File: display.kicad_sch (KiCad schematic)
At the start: 65 parts, among them IC11 SN74LV1T125DBVR, IC18 TPD8S009DSMR, IC2 TPD8S009DSMR, IC6 PCA9517ADP, J1 HDMI-Micro-D_Molex_467561001, J15 Bus_DDR4_SODIMM_CUSTOM_Jetson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, J2 DisplayPort-Mini_TE_2129320-3, T1 BSS138PW

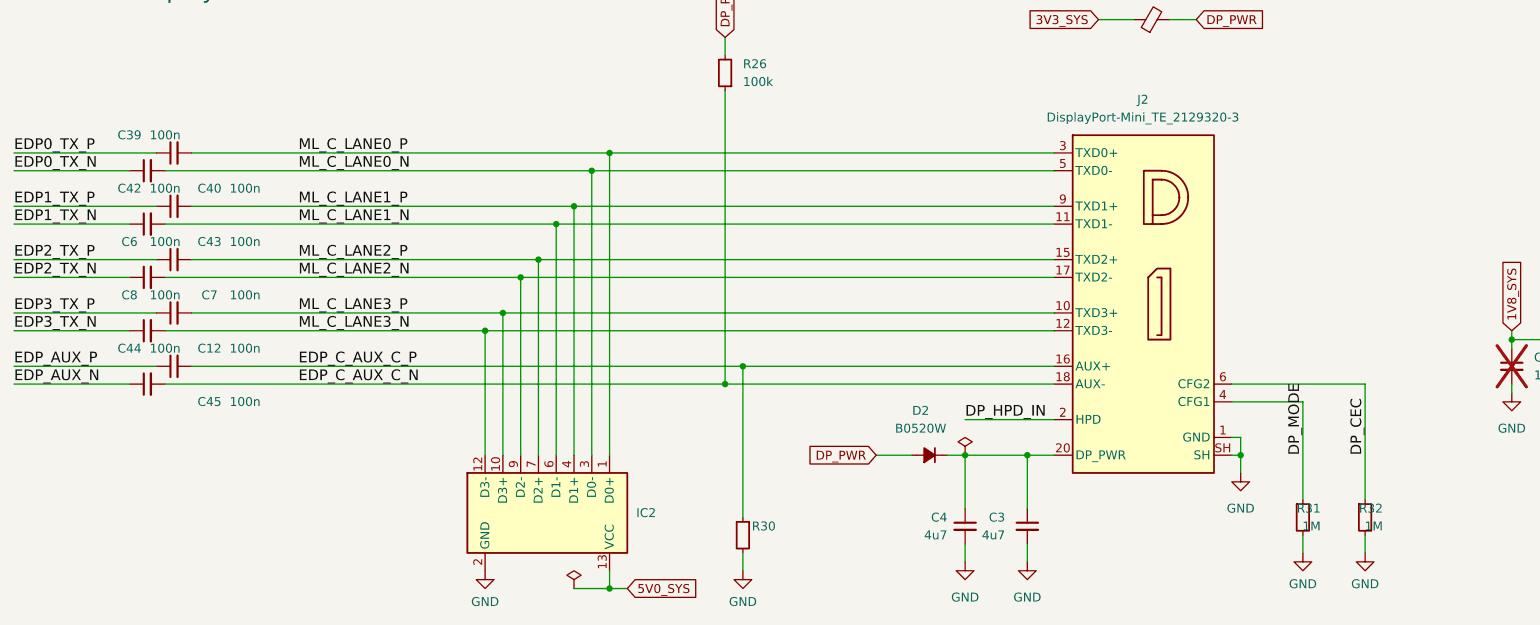
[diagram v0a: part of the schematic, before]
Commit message: fix(sch): resolve all symbol, label, property, and syntax collisions on Supply sheet (Page 6)
Fix unquoted COMP pin name in SIC477ED-T1-GE3, relocate #FLG0313 and #FLG0312 PWR_FLAGs, move R93/C61/R96/R76/R44/R70/L1/U1/U5/IC4/U3 properties out of bodies and wires, fix R117 table box, hide J4 duplicate Description, remove duplicate PWR_EN label and J12 MP1/MP2 no_connect conflicts, and delete stray off-sheet artifacts.

Co-Authored-By: CopperPilot <noreply@copperpilot.ai>
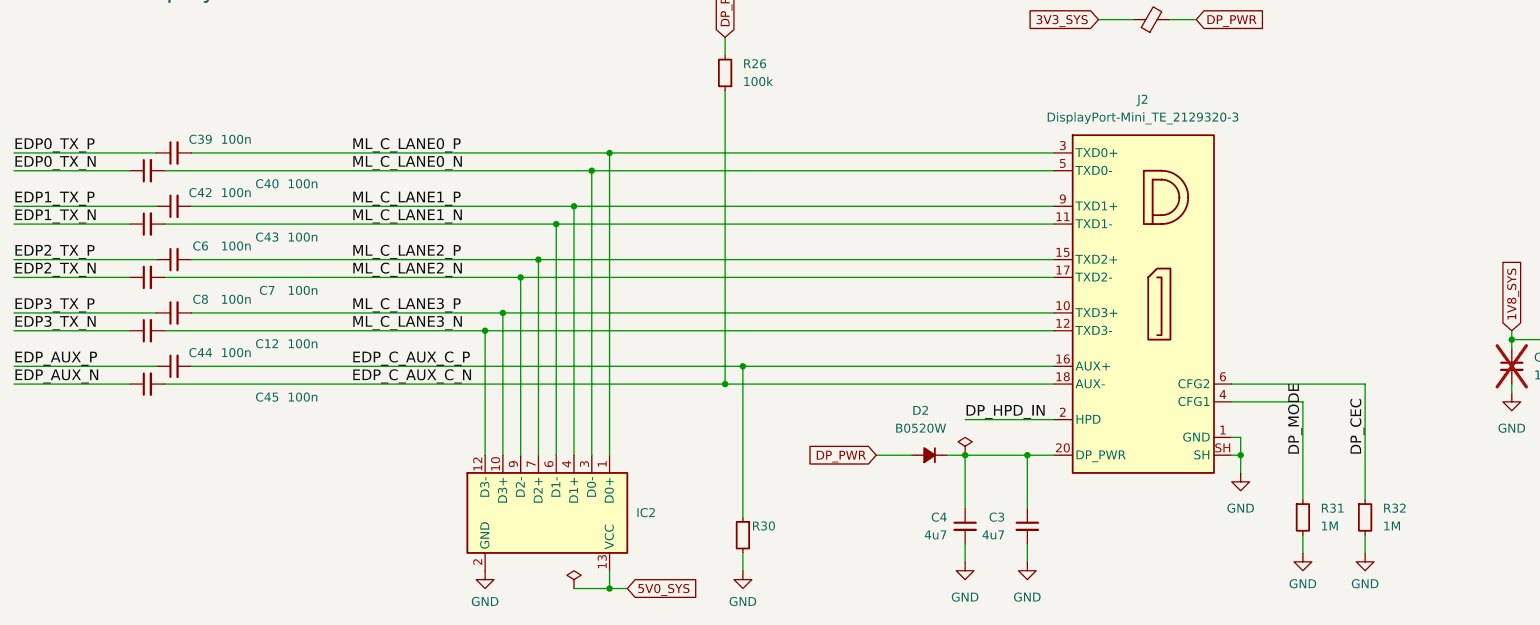
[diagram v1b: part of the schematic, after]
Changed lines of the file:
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@@
 		(dnp no)
 		(property "Reference" "C39"
-			(at 31.75 184.15 0)
+			(at 41.91 184.785 0)
 			(show_name no)
 			(do_not_autoplace no)
@@
 		)
 		(property "Val" "100n"
-			(at 36.83 184.15 0)
+			(at 46.99 184.785 0)
 			(show_name no)
 			(do_not_autoplace no)
@@
 		(dnp no)
 		(property "Reference" "C42"
-			(at 31.75 191.77 0)
+			(at 41.91 192.405 0)
 			(show_name no)
 			(do_not_autoplace no)
@@
 		)
 		(property "Val" "100n"
-			(at 36.83 191.77 0)
+			(at 46.99 192.405 0)
 			(show_name no)
 			(do_not_autoplace no)
@@
 		(dnp no)
 		(property "Reference" "C6"
-			(at 31.75 199.39 0)
+			(at 41.91 200.025 0)
 			(show_name no)
 			(do_not_autoplace no)
@@
 		)
 		(property "Val" "100n"
-			(at 36.83 199.39 0)
+			(at 46.99 200.025 0)
 			(show_name no)
 			(do_not_autoplace no)
@@
 		(dnp no)
 		(property "Reference" "C8"
-			(at 31.75 207.01 0)
+			(at 41.91 207.645 0)
 			(show_name no)
 			(do_not_autoplace no)
@@
 		)
 		(property "Val" "100n"
-			(at 36.83 207.01 0)
+			(at 46.99 207.645 0)
 			(show_name no)
 			(do_not_autoplace no)
@@
 		(dnp no)
 		(property "Reference" "C44"
-			(at 31.75 214.63 0)
+			(at 41.91 215.265 0)
 			(show_name no)
 			(do_not_autoplace no)
@@
 		)
 		(property "Val" "100n"
-			(at 36.83 214.63 0)
+			(at 46.99 215.265 0)
 			(show_name no)
 			(do_not_autoplace no)
@@
 		(dnp no)
 		(property "Reference" "C40"
-			(at 43.18 191.77 0)
+			(at 51.435 191.135 0)
 			(show_name no)
 			(do_not_autoplace no)
@@
 		)
 		(property "Val" "100n"
-			(at 48.26 191.77 0)
+			(at 56.515 191.135 0)
 			(show_name no)
 			(do_not_autoplace no)
@@
 		(dnp no)
 		(property "Reference" "C43"
-			(at 43.18 199.39 0)
+			(at 51.435 198.755 0)
 			(show_name no)
 			(do_not_autoplace no)
@@
 		)
 		(property "Val" "100n"
-			(at 48.26 199.39 0)
+			(at 56.515 198.755 0)
 			(show_name no)
 			(do_not_autoplace no)
@@
 		(dnp no)
 		(property "Reference" "C7"
-			(at 43.18 207.01 0)
+			(at 51.435 206.375 0)
 			(show_name no)
 			(do_not_autoplace no)
@@
 		)
 		(property "Val" "100n"
-			(at 48.26 207.01 0)
+			(at 56.515 206.375 0)
 			(show_name no)
 			(do_not_autoplace no)
@@
 		(dnp no)
 		(property "Reference" "C12"
-			(at 43.18 214.63 0)
+			(at 51.435 213.995 0)
 			(show_name no)
 			(do_not_autoplace no)
@@
 		)
 		(property "Val" "100n"
-			(at 48.26 214.63 0)
+			(at 56.515 213.995 0)
 			(show_name no)
 			(do_not_autoplace no)
@@
 		(dnp no)
 		(property "Reference" "C45"
-			(at 43.18 222.25 0)
+			(at 51.435 221.615 0)
 			(show_name no)
 			(do_not_autoplace no)
@@
 		)
 		(property "Val" "100n"
-			(at 48.26 222.25 0)
+			(at 56.515 221.615 0)
 			(show_name no)
 			(do_not_autoplace no)
@@
 					(thickness 0.15)
 				)
-				(justify left)
+				(justify right)
 			)
 		)
@@
 					(thickness 0.15)
 				)
-				(justify left)
+				(justify right)
 			)
 		)
@@
 					(thickness 0.15)
 				)
-				(justify left)
+				(justify right)
 			)
 		)
@@
 					(thickness 0.15)
 				)
-				(justify left)
+				(justify right)
 			)
 		)
@@
 	)
 	(label "ML_C_LANE0_P"
-		(at 55.88 186.69 0)
+		(at 63.5 186.69 0)
 		(effects
 			(font
@@
 	)
 	(label "ML_C_LANE3_P"
-		(at 55.88 209.55 0)
+		(at 63.5 209.55 0)
 		(effects
 			(font
@@
 	)
 	(label "ML_C_LANE1_N"
-		(at 55.88 196.85 0)
+		(at 63.5 196.85 0)
 		(effects
 			(font
@@
 	)
 	(label "EDP_C_AUX_C_P"
-		(at 55.88 217.17 0)
+		(at 63.5 217.17 0)
 		(effects
 			(font
@@
 	)
 	(label "ML_C_LANE0_N"
-		(at 55.88 189.23 0)
+		(at 63.5 189.23 0)
 		(effects
 			(font
@@
 	)
 	(label "EDP_C_AUX_C_N"
-		(at 55.88 219.71 0)
+		(at 63.5 219.71 0)
 		(effects
 			(font
@@
 	)
 	(label "ML_C_LANE1_P"
-		(at 55.88 194.31 0)
+		(at 63.5 194.31 0)
 		(effects
 			(font
@@
 	)
 	(label "ML_C_LANE2_N"
-		(at 55.88 204.47 0)
+		(at 63.5 204.47 0)
 		(effects
 			(font
@@
 	)
 	(label "ML_C_LANE2_P"
-		(at 55.88 201.93 0)
+		(at 63.5 201.93 0)
 		(effects
 			(font
@@
 	)
 	(label "ML_C_LANE3_N"
-		(at 55.88 212.09 0)
+		(at 63.5 212.09 0)
 		(effects
 			(font

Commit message: fix(bom): update LCSC procurement part numbers and SMT assembly flags
Reconcile LCSC part numbers with physical land patterns and active stock:
- J11 USB-C: C456013 (24-pin SuperSpeed receptacle matching Wurth 632723300011)
- J15 SODIMM: C2766246 (TE 2309413-1 260-pin socket)
- J2 Mini-DP: C574827 (TE 2129320-3)
- J1 Micro-HDMI: C563878 (Molex 467651001)
- J5, J9 Micro-USB: C132560 (Molex 473460001)
- REC1, RST1, USR1: C2886925 (E-Switch TL3340AF160QG)
- BAT1: set DNP for SMT reflow to prevent thermal rupture in 260C oven

Co-Authored-By: CopperPilot <noreply@copperpilot.ai>
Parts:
- J1: LCSC C168694 -> C563878
- J15: LCSC C429199 -> C2766246
- J2: LCSC C511423 -> C574827
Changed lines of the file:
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@@
 			)
 		)
-		(property "LCSC" "C429199"
+		(property "LCSC" "C2766246"
 			(at 0 0 0)
 			(effects
@@
 			)
 		)
-		(property "LCSC" "C168694"
+		(property "LCSC" "C563878"
 			(at 0 0 0)
 			(effects
@@
 			)
 		)
-		(property "LCSC" "C511423"
+		(property "LCSC" "C574827"
 			(at 0 0 0)
 			(effects

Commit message: fix(sch,pcb): populate level translator decoupling bypass capacitor C5
Remove DNP exclusion from 100nF bypass capacitor C5 on display interface level translator IC11 (SN74LV1T125) on schematic and PCB layout, adding C5 to production BOM with LCSC C1525.

Co-Authored-By: CopperPilot <noreply@copperpilot.ai>
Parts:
- C5: now fitted; now in the parts list
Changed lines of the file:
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@@
 		(body_style 1)
 		(exclude_from_sim no)
-		(in_bom no)
+		(in_bom yes)
 		(on_board yes)
 		(in_pos_files yes)
-		(dnp yes)
+		(dnp no)
 		(fields_autoplaced yes)
 		(property "Reference" "C5"
